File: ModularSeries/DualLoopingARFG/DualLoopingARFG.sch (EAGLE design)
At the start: 63 parts, among them IC1 TL084P, IC2 TL084P, Q1 2N3904, Q2 2N3904

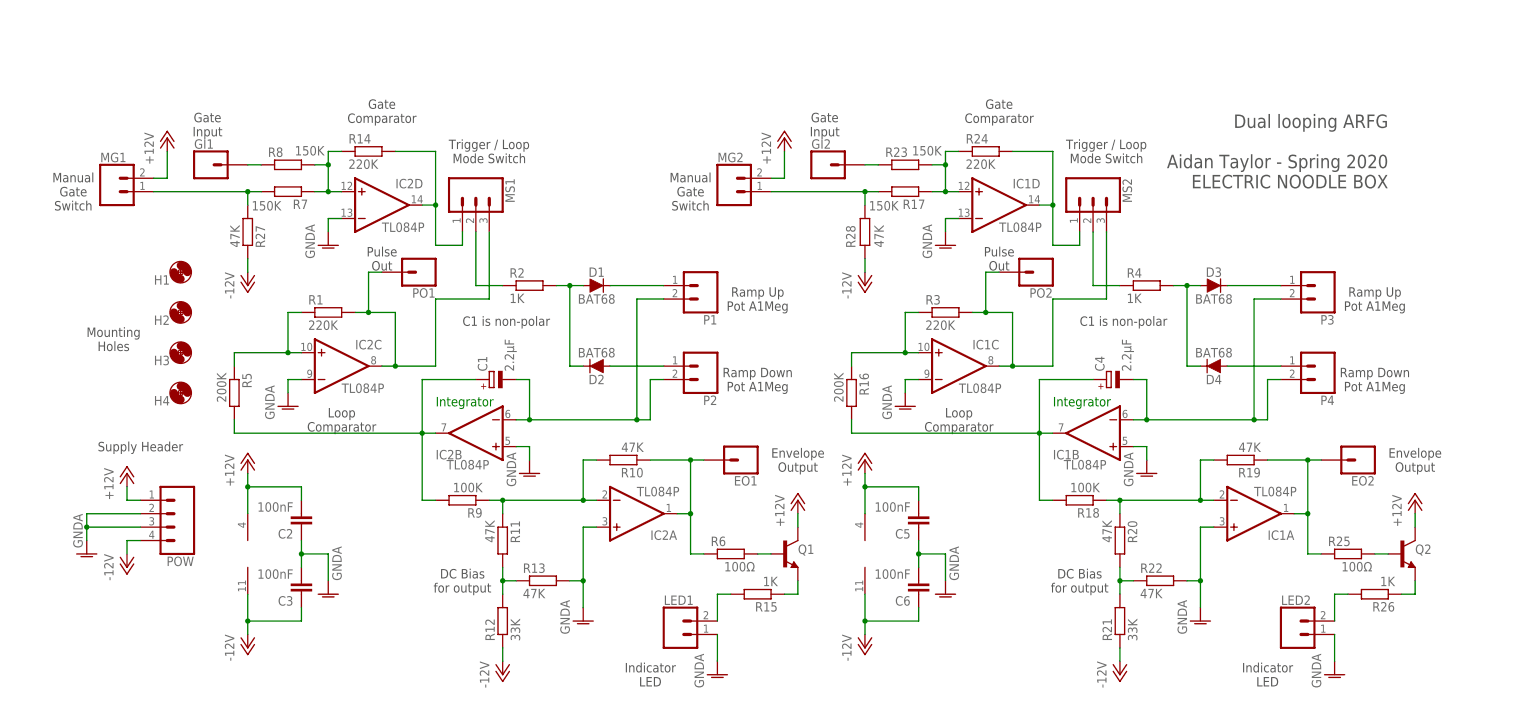
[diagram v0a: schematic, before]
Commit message: All PCBs now use unified library, Eagle library added
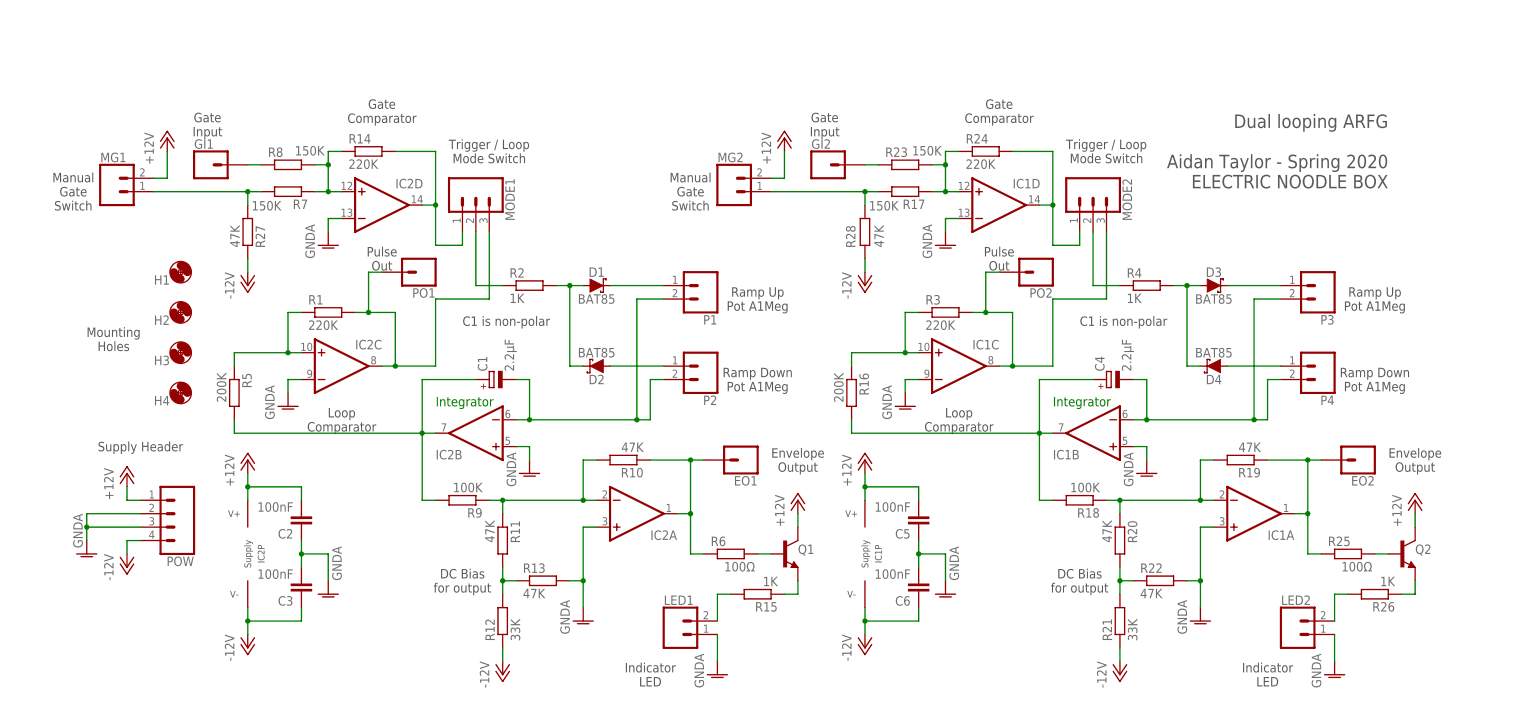
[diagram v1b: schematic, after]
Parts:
- removed MS1, MS2: (no value), SparkFun-Connectors:CONN_03
- added MODE1, MODE2: 3XWIREPAD, ElectricNoodleBox:3XWIREPAD
- D1, D2, D3, D4: value BAT68 -> BAT85; device SparkFun-DiscreteSemi:DIODE-1N4148 -> ElectricNoodleBox:SCHOTTKY_DO35
- EO1, EO2, GI1, GI2, PO1, PO2: value (none) -> 1XWIREPAD; device SparkFun-Connectors:CONN_01 -> ElectricNoodleBox:1XWIREPAD
- IC1, IC2: value TL084P -> TL0X4_DIP; device linear:TL084P -> ElectricNoodleBox:TL0X4_DIP
- LED1, LED2, MG1, MG2, P1, P2, P3, P4: value (none) -> 2XWIREPAD; device SparkFun-Connectors:CONN_02 -> ElectricNoodleBox:2XWIREPAD
- POW: value (none) -> 4XMOLEX; device SparkFun-Connectors:CONN_04POLAR -> ElectricNoodleBox:4XMOLEX
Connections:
- net N$1: now also MODE1.3; no longer MS1.3
- net N$14: now also MODE1.2; no longer MS1.2
- net N$15: now also MODE1.1; no longer MS1.1
- net N$17: now also MODE2.3; no longer MS2.3
- net N$27: now also MODE2.1; no longer MS2.1
- net N$28: now also MODE2.2; no longer MS2.2

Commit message: Library updated, variants consolidated
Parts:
- IC1, IC2: value TL0X4_DIP -> (none); device ElectricNoodleBox:TL0X4_DIP -> ElectricNoodleBox:TL0X4DIL
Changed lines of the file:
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@@
 <part name="EO1" library="ElectricNoodleBox" deviceset="1XWIREPAD" device=""/>
 <part name="LED1" library="ElectricNoodleBox" deviceset="2XWIREPAD" device=""/>
-<part name="IC2" library="ElectricNoodleBox" deviceset="TL0X4_DIP" device="" package3d_urn="urn:adsk.eagle:package:16407/2"/>
+<part name="IC2" library="ElectricNoodleBox" deviceset="TL0X4" device="DIL" package3d_urn="urn:adsk.eagle:package:16407/2"/>
 <part name="R3" library="rcl" library_urn="urn:adsk.eagle:library:334" deviceset="R-EU_" device="0207/10" package3d_urn="urn:adsk.eagle:package:23491/2" value="220K"/>
 <part name="C4" library="rcl" library_urn="urn:adsk.eagle:library:334" deviceset="CPOL-EU" device="E2-5" package3d_urn="urn:adsk.eagle:package:23346/2" value="2.2µF"/>
@@
 <part name="EO2" library="ElectricNoodleBox" deviceset="1XWIREPAD" device=""/>
 <part name="LED2" library="ElectricNoodleBox" deviceset="2XWIREPAD" device=""/>
-<part name="IC1" library="ElectricNoodleBox" deviceset="TL0X4_DIP" device="" package3d_urn="urn:adsk.eagle:package:16407/2"/>
+<part name="IC1" library="ElectricNoodleBox" deviceset="TL0X4" device="DIL" package3d_urn="urn:adsk.eagle:package:16407/2"/>
 <part name="POW" library="ElectricNoodleBox" deviceset="4XMOLEX" device="">
 <attribute name="SPICEPREFIX" value="E"/>

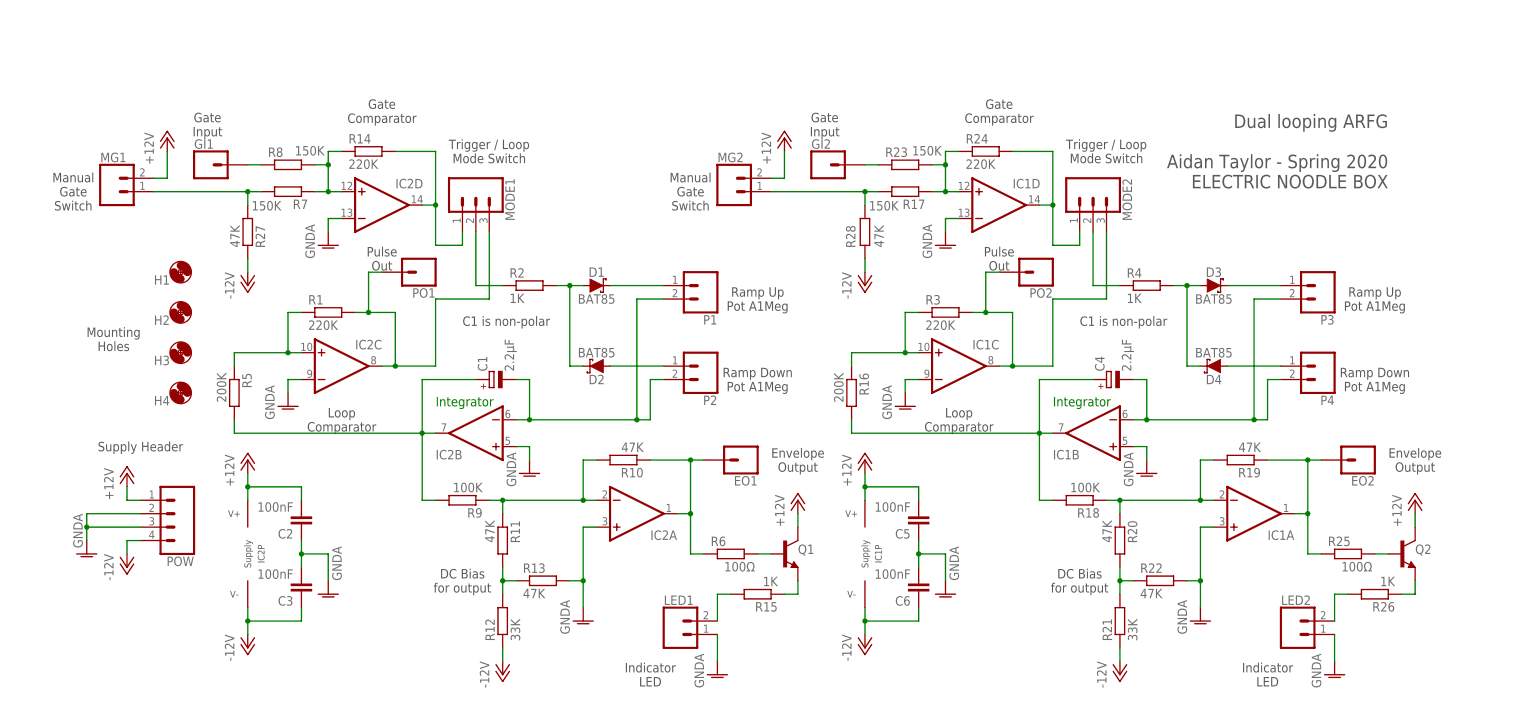
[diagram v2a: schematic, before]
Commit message: Updates to ARFG schematic - not included in layout yet
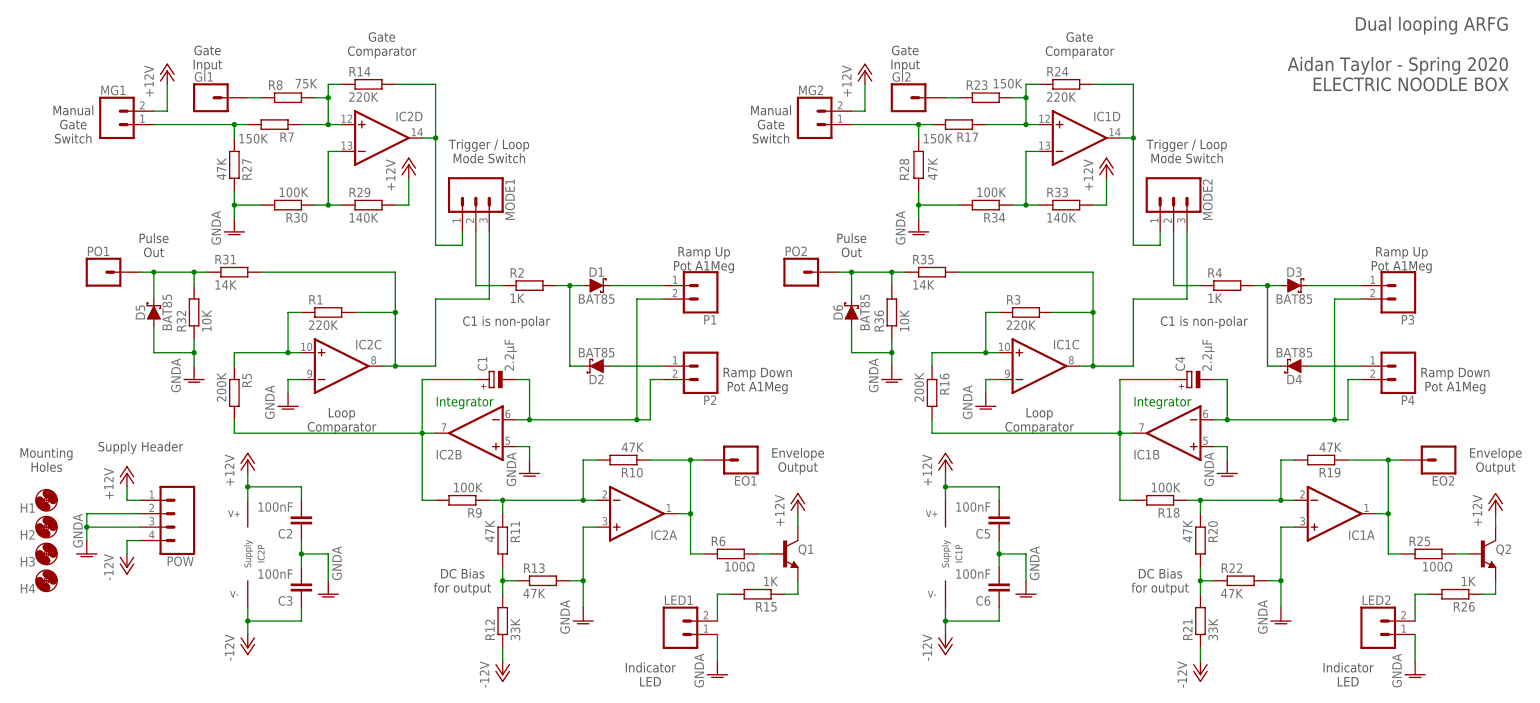
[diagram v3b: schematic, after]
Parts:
- added D5, D6: BAT85, ElectricNoodleBox:SCHOTTKY_DO35
- added R29, R33: 140K, rcl:R-EU_0207/10
- added R30, R34: 100K, rcl:R-EU_0207/10
- added R31, R35: 14K, rcl:R-EU_0207/10
- added R32, R36: 10K, rcl:R-EU_0207/10
- R8: value 150K -> 75K
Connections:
- new net N$33: IC2D.-IN, R29.1, R30.1
- new net N$34: D5.C, PO1.1, R31.1, R32.2
- new net N$35: IC1D.-IN, R33.1, R34.1
- new net N$36: D6.C, PO2.1, R35.1, R36.2
- net +12V: now also R29.2, R33.2
- net -12V: no longer R27.2, R28.2
- net GNDA: now also D5.A, D6.A, R27.2, R28.2, R30.2, R32.1, R34.2, R36.1; no longer IC1D.-IN, IC2D.-IN
- net N$1: now also R31.2; no longer PO1.1
- net N$17: now also R35.2; no longer PO2.1
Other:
- moved on the sheet: C4, C5, C6, D3, D4, EO2, GI1, GI2, H1, H2, H3, H4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
